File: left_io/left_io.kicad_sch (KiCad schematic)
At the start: 0 parts

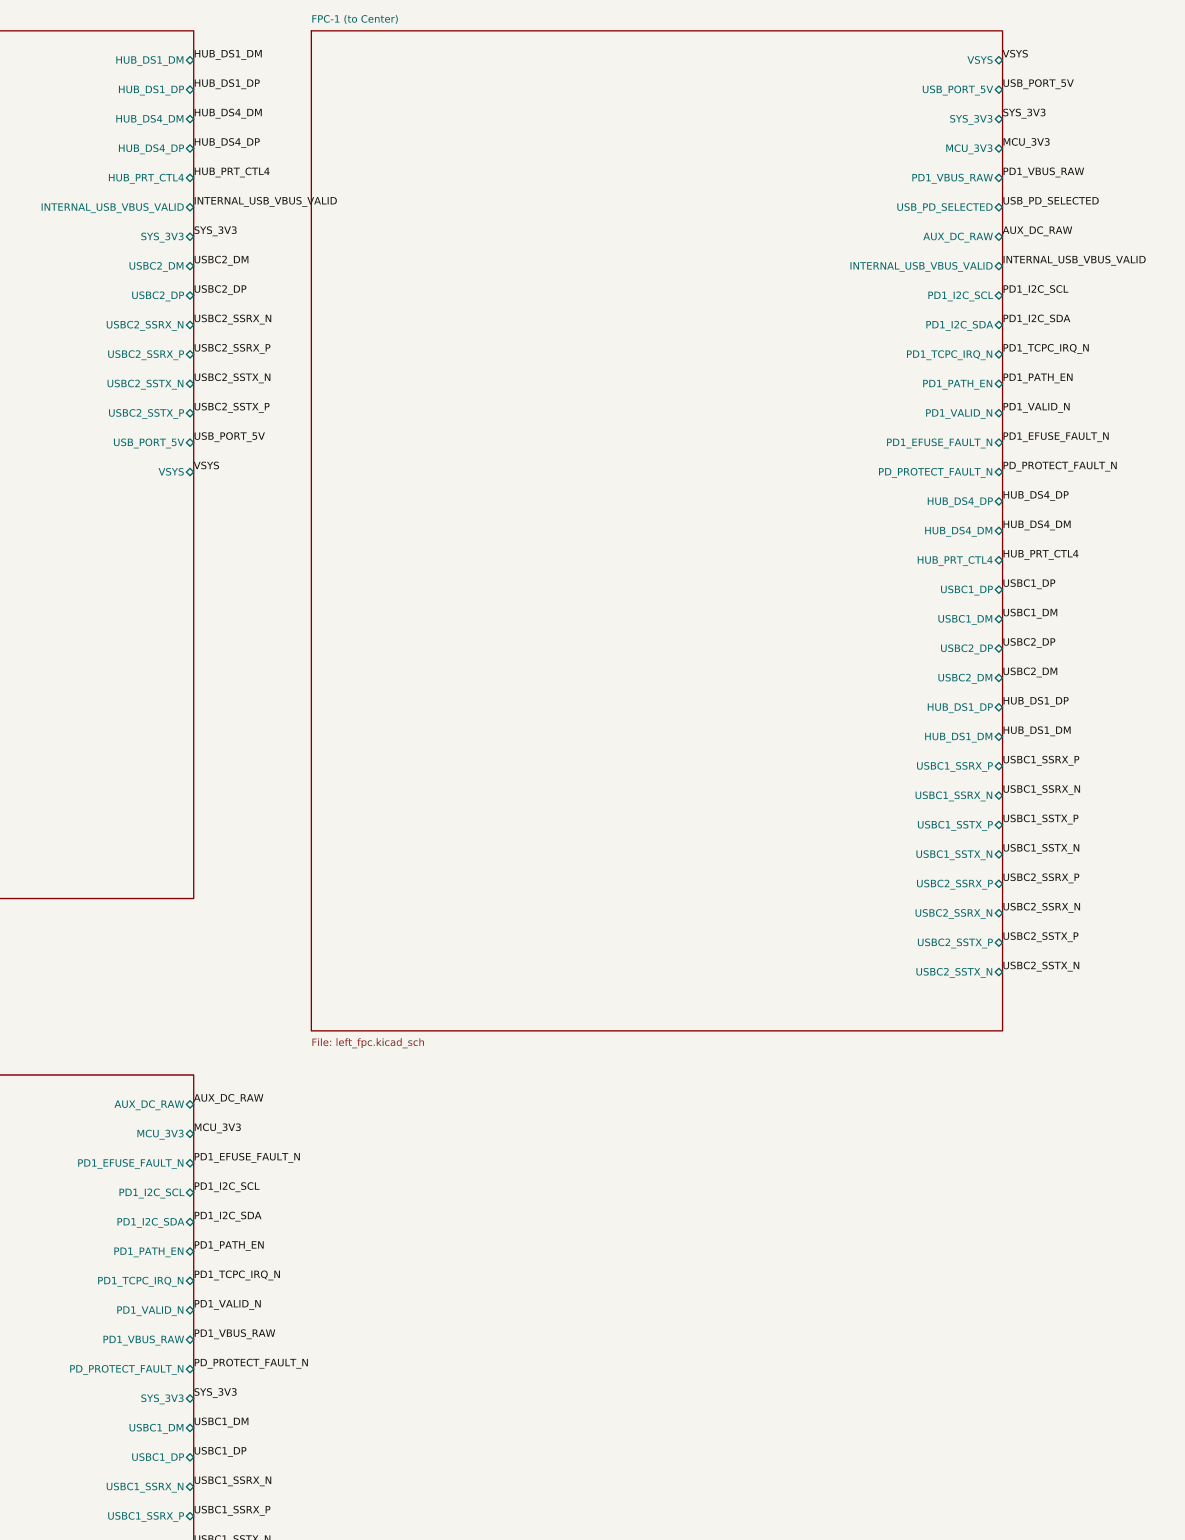
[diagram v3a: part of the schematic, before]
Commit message: get the main boards ready for routing
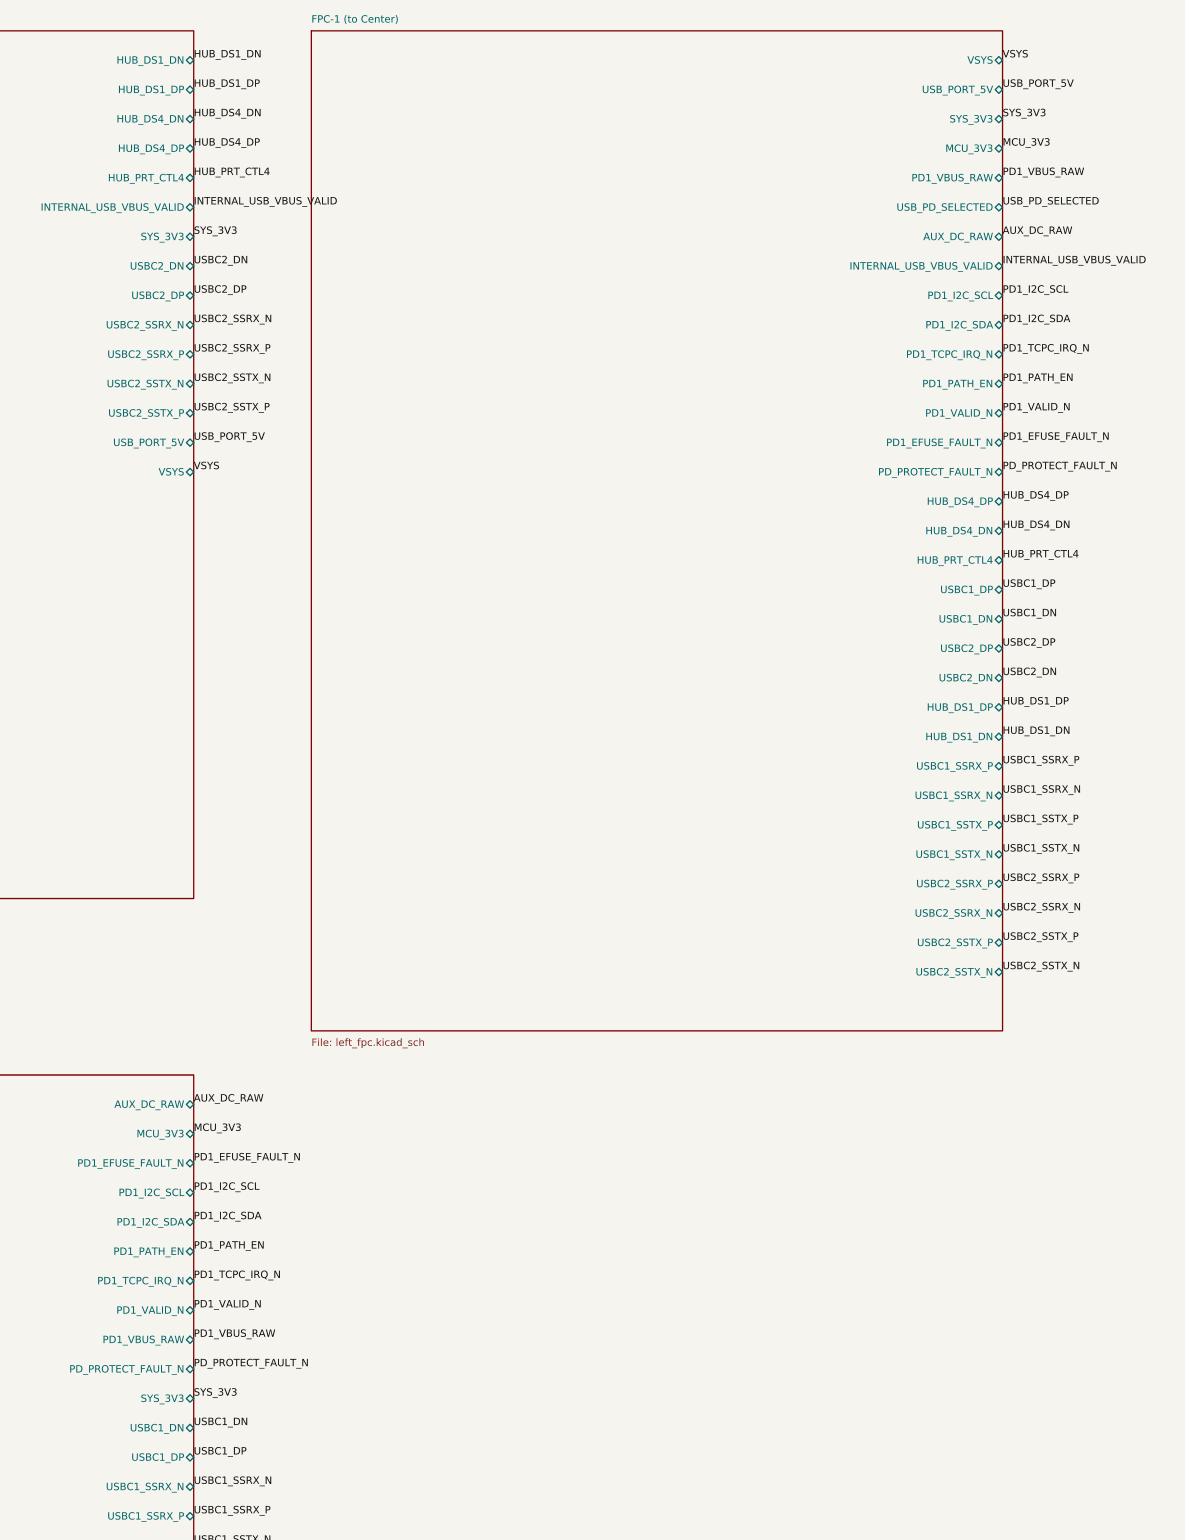
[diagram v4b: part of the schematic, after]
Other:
- sheet FPC-1 (to Center) ports: added HUB_DS1_DN, HUB_DS4_DN, USBC1_DN, USBC2_DN; removed HUB_DS1_DM, HUB_DS4_DM, USBC1_DM, USBC2_DM
- sheet PD1 Dual-Role ports: added USBC1_DN; removed USBC1_DM
- sheet USB Hub + Ports ports: added HUB_DS1_DN, HUB_DS4_DN, USBC2_DN; removed HUB_DS1_DM, HUB_DS4_DM, USBC2_DM
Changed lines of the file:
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@@
     (effects (font (size 1.27 1.27)) (justify left top))
   )
-  (pin "HUB_DS1_DM" bidirectional
+  (pin "HUB_DS1_DN" bidirectional
     (at 149.86 44.45 0)
     (effects (font (size 1.27 1.27)) (justify left))
@@
     (effects (font (size 1.27 1.27)) (justify left))
   )
-  (pin "HUB_DS4_DM" bidirectional
+  (pin "HUB_DS4_DN" bidirectional
     (at 149.86 54.61 0)
     (effects (font (size 1.27 1.27)) (justify left))
@@
     (effects (font (size 1.27 1.27)) (justify left))
   )
-  (pin "USBC2_DM" bidirectional
+  (pin "USBC2_DN" bidirectional
     (at 149.86 80.01 0)
     (effects (font (size 1.27 1.27)) (justify left))
@@
     (effects (font (size 1.27 1.27)) (justify left))
   )
-  (pin "USBC1_DM" bidirectional
+  (pin "USBC1_DN" bidirectional
     (at 149.86 280.67 0)
     (effects (font (size 1.27 1.27)) (justify left))
@@
     (effects (font (size 1.27 1.27)) (justify left))
   )
-  (pin "HUB_DS4_DM" bidirectional
+  (pin "HUB_DS4_DN" bidirectional
     (at 289.56 125.73 0)
     (effects (font (size 1.27 1.27)) (justify left))
@@
     (effects (font (size 1.27 1.27)) (justify left))
   )
-  (pin "USBC1_DM" bidirectional
+  (pin "USBC1_DN" bidirectional
     (at 289.56 140.97 0)
     (effects (font (size 1.27 1.27)) (justify left))
@@
     (effects (font (size 1.27 1.27)) (justify left))
   )
-  (pin "USBC2_DM" bidirectional
+  (pin "USBC2_DN" bidirectional
     (at 289.56 151.13 0)
     (effects (font (size 1.27 1.27)) (justify left))
@@
     (effects (font (size 1.27 1.27)) (justify left))
   )
-  (pin "HUB_DS1_DM" bidirectional
+  (pin "HUB_DS1_DN" bidirectional
     (at 289.56 161.29 0)
     (effects (font (size 1.27 1.27)) (justify left))
@@
   )
 )
-(label "HUB_DS1_DM"
+(label "HUB_DS1_DN"
   (at 149.86 44.45 0)
   (effects (font (size 1.27 1.27)) (justify left bottom))
@@
   (effects (font (size 1.27 1.27)) (justify left bottom))
 )
-(label "HUB_DS4_DM"
+(label "HUB_DS4_DN"
   (at 149.86 54.61 0)
   (effects (font (size 1.27 1.27)) (justify left bottom))
@@
   (effects (font (size 1.27 1.27)) (justify left bottom))
 )
-(label "USBC2_DM"
+(label "USBC2_DN"
   (at 149.86 80.01 0)
   (effects (font (size 1.27 1.27)) (justify left bottom))
@@
   (effects (font (size 1.27 1.27)) (justify left bottom))
 )
-(label "USBC1_DM"
+(label "USBC1_DN"
   (at 149.86 280.67 0)
   (effects (font (size 1.27 1.27)) (justify left bottom))
@@
   (effects (font (size 1.27 1.27)) (justify left bottom))
 )
-(label "HUB_DS4_DM"
+(label "HUB_DS4_DN"
   (at 289.56 125.73 0)
   (effects (font (size 1.27 1.27)) (justify left bottom))
@@
   (effects (font (size 1.27 1.27)) (justify left bottom))
 )
-(label "USBC1_DM"
+(label "USBC1_DN"
   (at 289.56 140.97 0)
   (effects (font (size 1.27 1.27)) (justify left bottom))
@@
   (effects (font (size 1.27 1.27)) (justify left bottom))
 )
-(label "USBC2_DM"
+(label "USBC2_DN"
   (at 289.56 151.13 0)
   (effects (font (size 1.27 1.27)) (justify left bottom))
@@
   (effects (font (size 1.27 1.27)) (justify left bottom))
 )
-(label "HUB_DS1_DM"
+(label "HUB_DS1_DN"
   (at 289.56 161.29 0)
   (effects (font (size 1.27 1.27)) (justify left bottom))

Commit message: fix more power stuff and update the left board
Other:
- sheet FPC-1 (to Center) ports: added PD2_SOURCE_PG, SERVICE_MUX_RESET_N, USB_J11_PERMIT, USB_J12_PERMIT; removed none
- sheet PD1 Dual-Role ports: added PD1_SOURCE_PG, USB_J21_PERMIT; removed none
- sheet USB Hub + Ports ports: added MCU_3V3, PD1_I2C_SCL, PD1_I2C_SDA, PD1_SOURCE_PG, PD2_SOURCE_PG, SERVICE_MUX_RESET_N, USB_J11_PERMIT, USB_J12_PERMIT, USB_J21_PERMIT; removed none

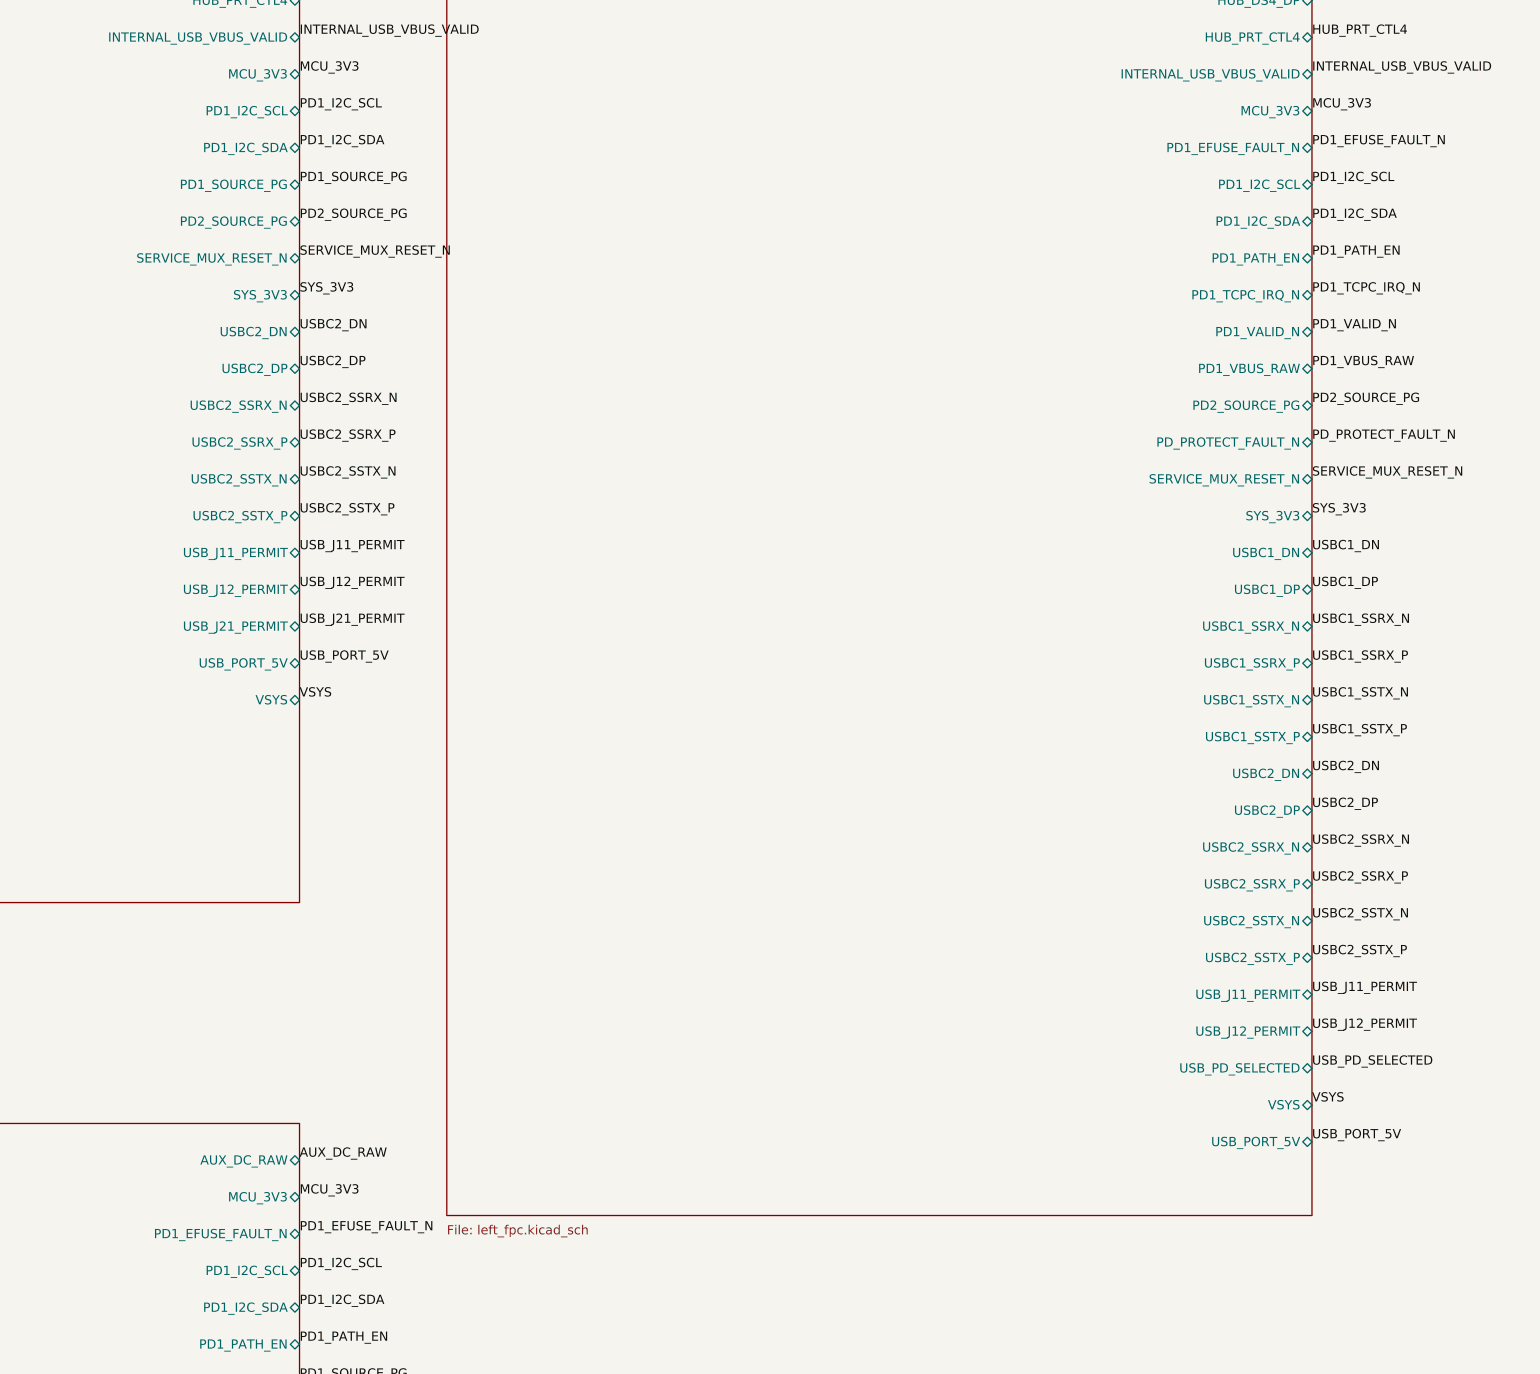
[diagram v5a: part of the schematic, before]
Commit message: rework the board placement and fix more power stuff
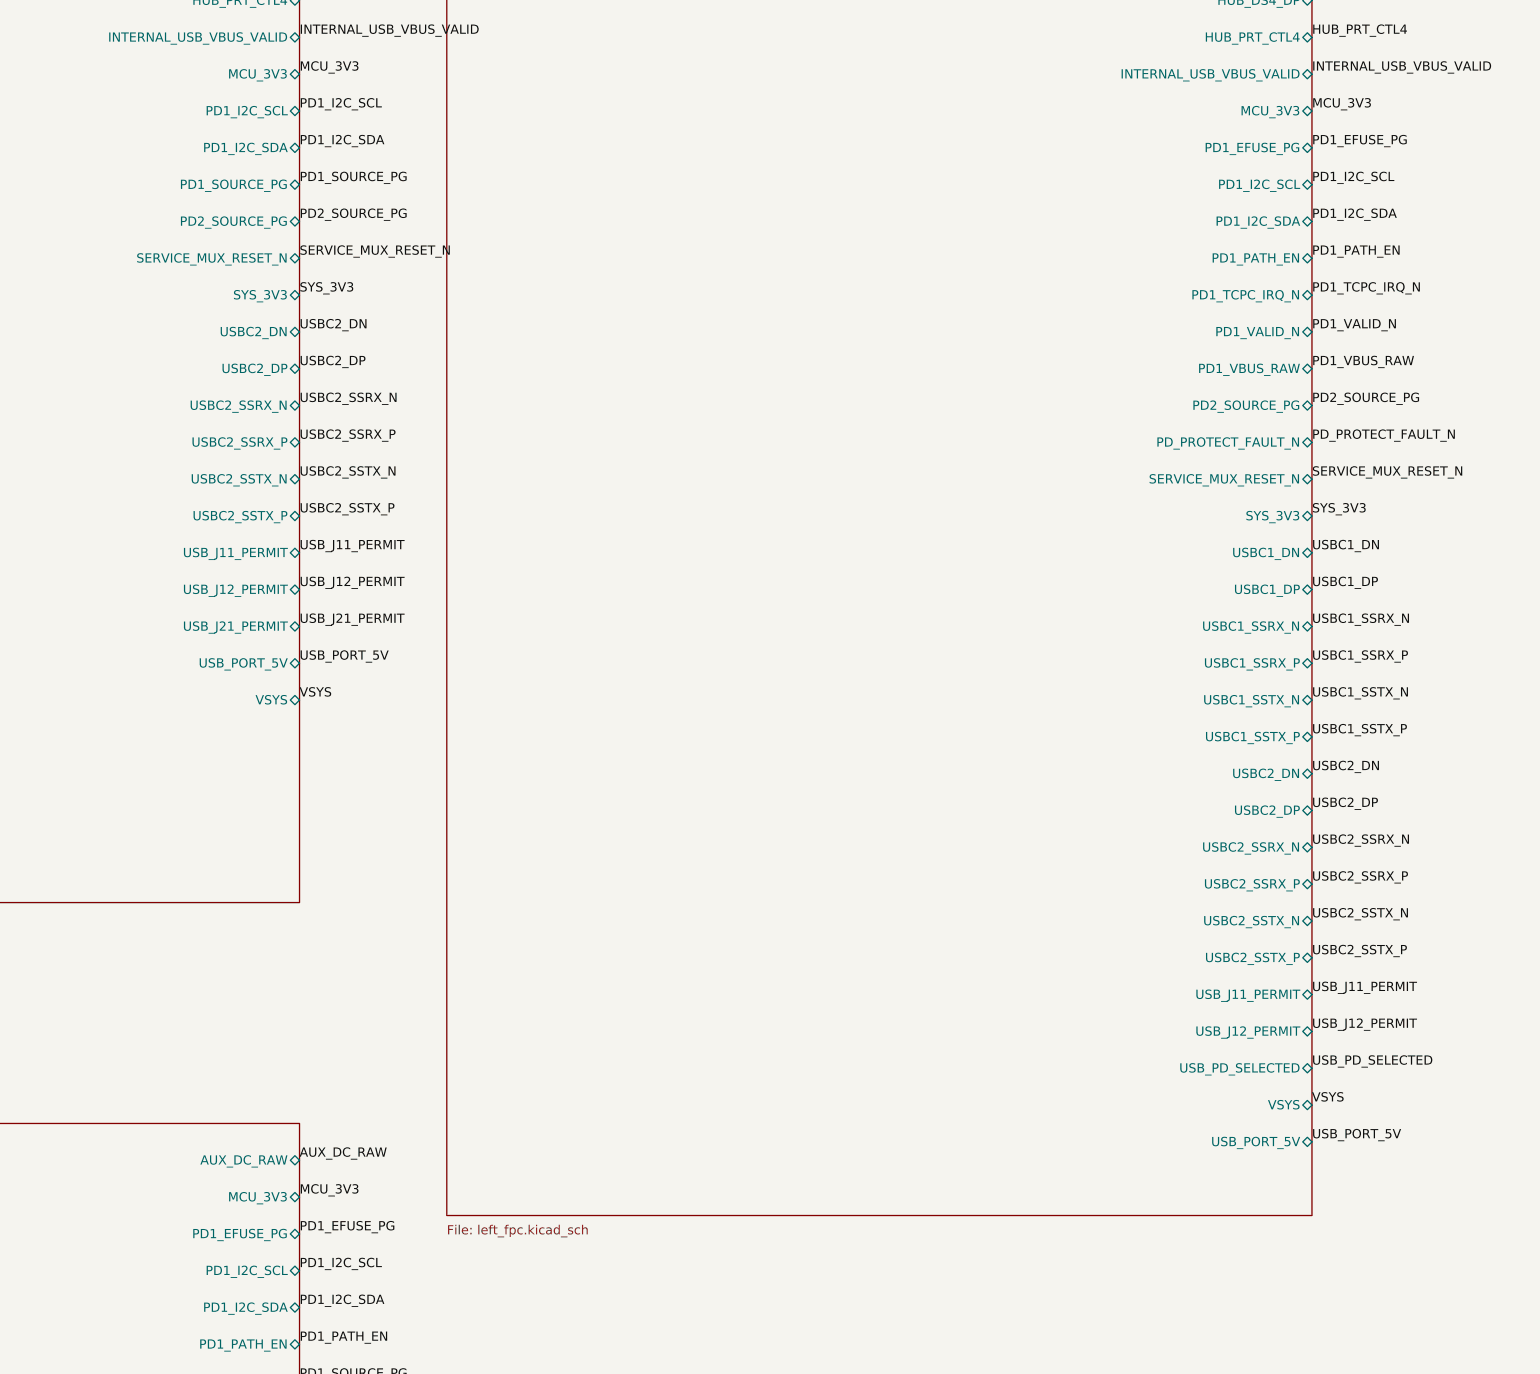
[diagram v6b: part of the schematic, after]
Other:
- sheet FPC-1 (to Center) ports: added PD1_EFUSE_PG; removed PD1_EFUSE_FAULT_N
- sheet PD1 Dual-Role ports: added PD1_EFUSE_PG; removed PD1_EFUSE_FAULT_N
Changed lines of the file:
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@@
 (sheet
   (at 30.48 39.37)
-  (size 119.38 149.86)
+  (size 119.38 149.8600)
   (stroke (width 0.1524) (type solid))
   (fill (color 0 0 0 0.0))
@@
 (sheet
   (at 30.48 219.71)
-  (size 119.38 149.86)
+  (size 119.38 149.8600)
   (stroke (width 0.1524) (type solid))
   (fill (color 0 0 0 0.0))
@@
     (effects (font (size 1.27 1.27)) (justify left))
   )
-  (pin "PD1_EFUSE_FAULT_N" bidirectional
+  (pin "PD1_EFUSE_PG" bidirectional
     (at 149.86 234.95 0)
     (effects (font (size 1.27 1.27)) (justify left))
@@
 (sheet
   (at 170.18 39.37)
-  (size 119.38 193.04)
+  (size 119.38 193.0400)
   (stroke (width 0.1524) (type solid))
   (fill (color 0 0 0 0.0))
@@
     (effects (font (size 1.27 1.27)) (justify left))
   )
-  (pin "PD1_EFUSE_FAULT_N" bidirectional
+  (pin "PD1_EFUSE_PG" bidirectional
     (at 289.56 85.09 0)
     (effects (font (size 1.27 1.27)) (justify left))
@@
   (effects (font (size 1.27 1.27)) (justify left bottom))
 )
-(label "PD1_EFUSE_FAULT_N"
+(label "PD1_EFUSE_PG"
   (at 149.86 234.95 0)
   (effects (font (size 1.27 1.27)) (justify left bottom))
@@
   (effects (font (size 1.27 1.27)) (justify left bottom))
 )
-(label "PD1_EFUSE_FAULT_N"
+(label "PD1_EFUSE_PG"
   (at 289.56 85.09 0)
   (effects (font (size 1.27 1.27)) (justify left bottom))
